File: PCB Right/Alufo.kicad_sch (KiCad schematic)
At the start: 32 parts, among them J2 USB_C_Receptacle_USB2.0_16P_2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, J4 USB_C_Receptacle_USB2.0_16P_2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, J6 SolderHole, SW2 BOOT, U2 CH552T, U4 USBLC6-2P6, U6 USBLC6-2P6

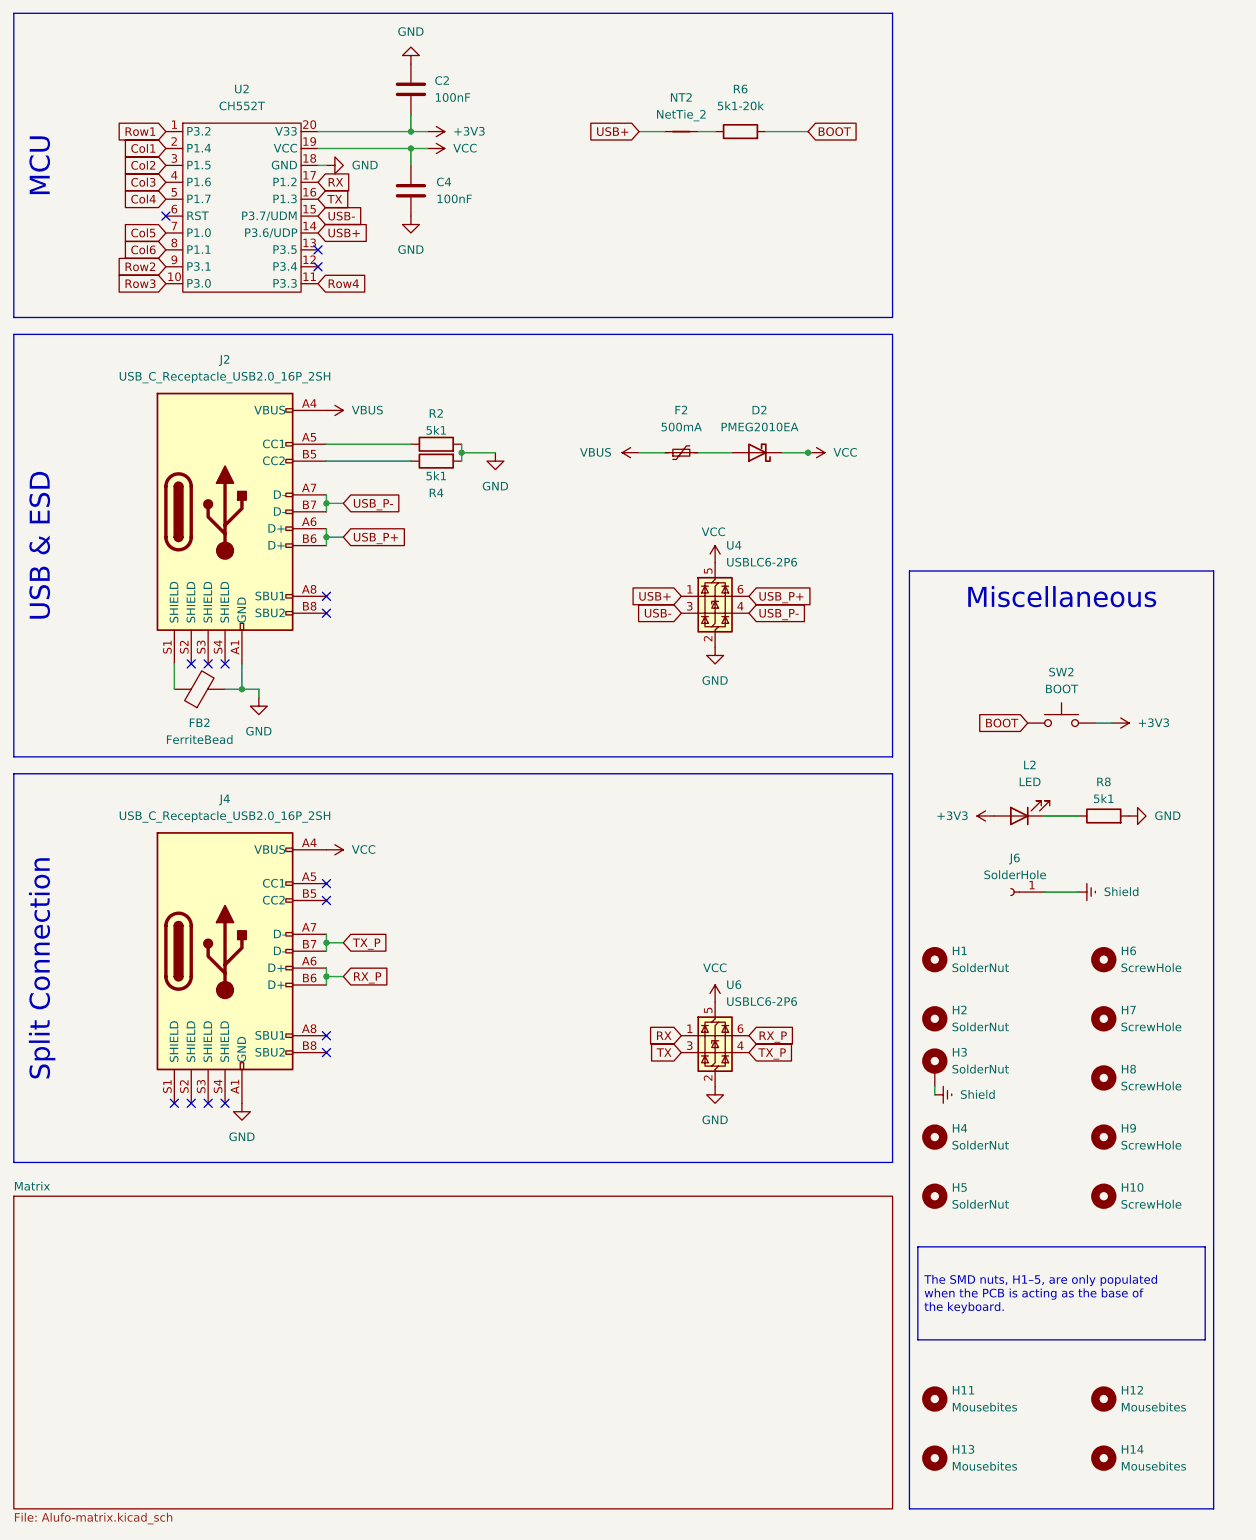
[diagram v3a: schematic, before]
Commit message: Update right side
Also add outline for middle layer to new USB port footprint (although it won’t be right.
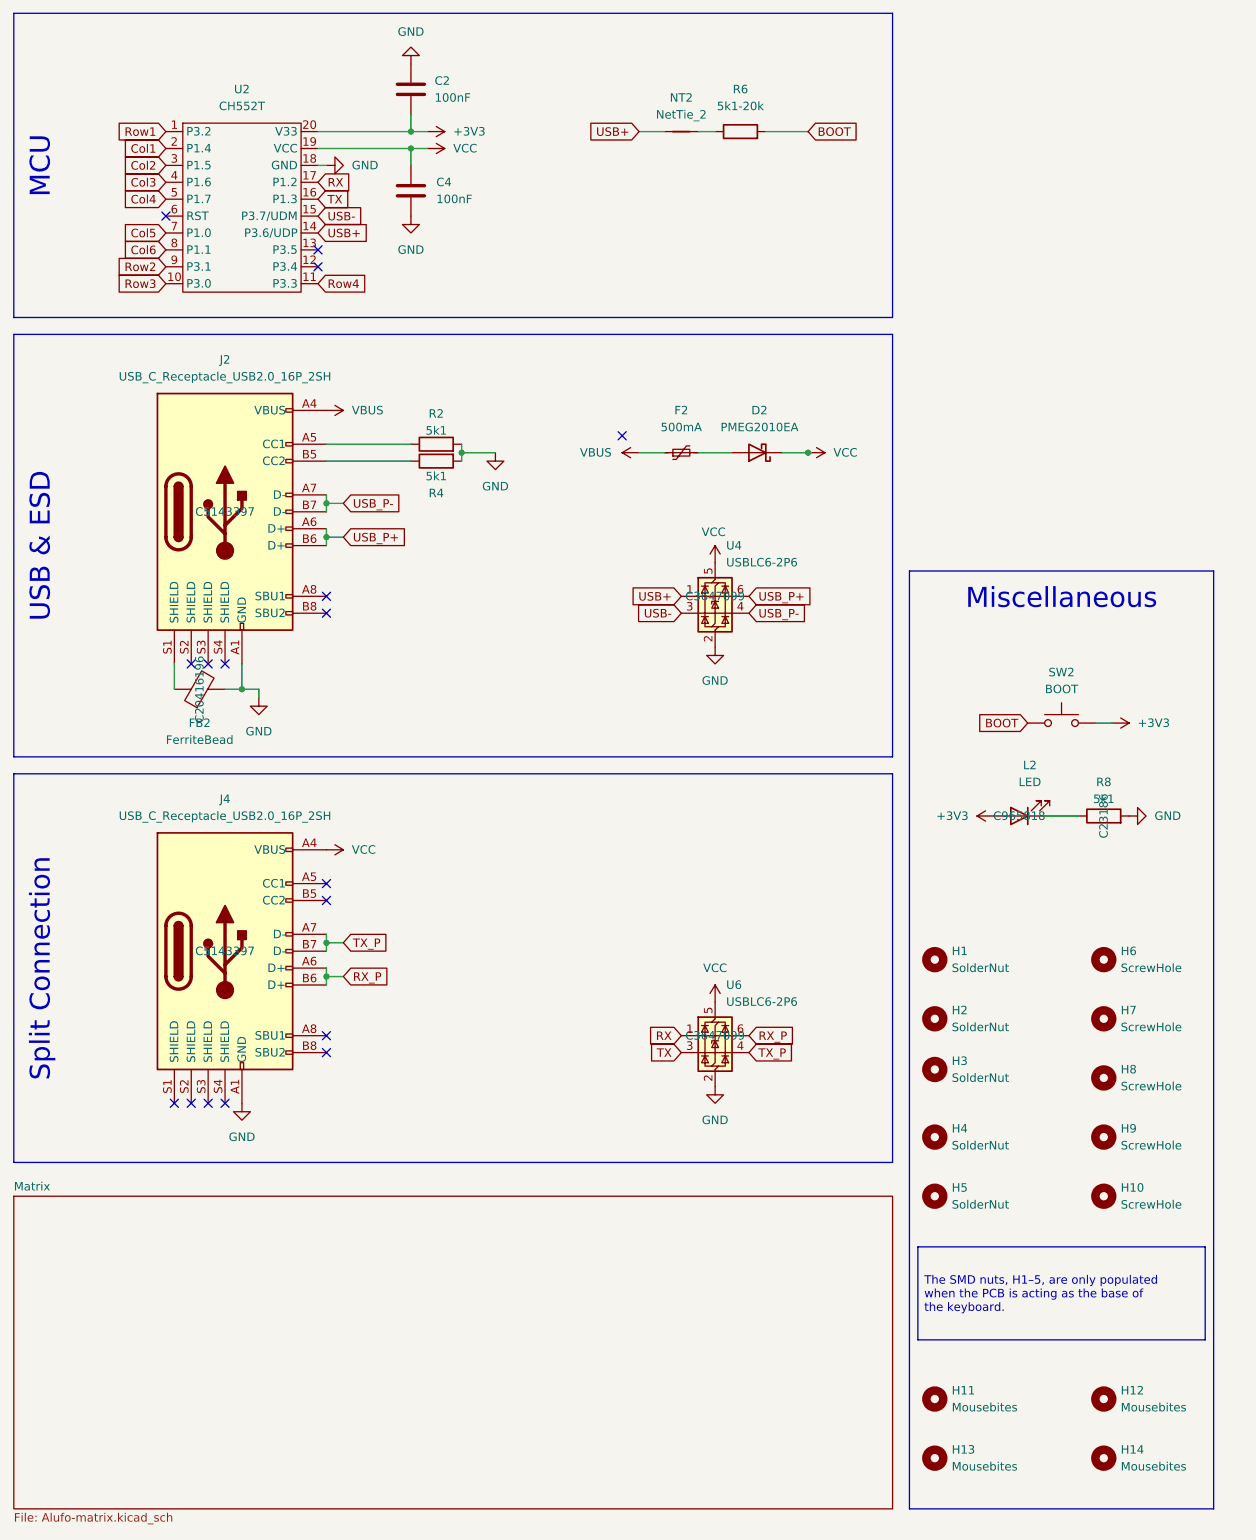
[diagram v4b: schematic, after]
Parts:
- removed J6: SolderHole, Project_Library:TestPoint_THTPad_D2.5mm_Drill1.2mm, symbol Connector:Conn_01x01_Socket
- D2: LCSC C2837790 -> C193668
- FB2: LCSC (none) -> C20416196
- H3: footprint Project_Library:MountingHole_2.2mm_M2_SMD_Solder_Nut_Pad -> Project_Library:MountingHole_2.2mm_M2_SMD_Solder_Nut; symbol Mechanical:MountingHole_Pad -> Mechanical:MountingHole; now left out of the parts list
- J2, J4: footprint Project_Library:USB_C_Receptacle_HRO_TYPE-C-31-M-12 -> Project_Library:USB_C_Receptacle_GCT_USB4110; LCSC (none) -> C5143397
- L2: LCSC (none) -> C965818
- R8: LCSC (none) -> C23186
- U4, U6: LCSC (none) -> C3647099
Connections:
- removed net Shield: H3.1
- no-connect marks 16 -> 17
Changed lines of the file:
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@@
 	(title_block
 		(title "Alufo ")
-		(rev "1.0R")
+		(rev "1.1R")
 		(company "bgkendall")
 		(comment 1 "Split one-layer reversible keyboard PCB (righthand side)")
@@
 	)
 	(no_connect
+		(at 106.68 88.9)
+	)
+	(no_connect
 		(at 62.23 156.21)
 	)
@@
 	(wire
 		(pts
-			(xy 153.67 186.69) (xy 153.67 187.96)
-		)
-		(stroke
-			(width 0)
-			(type default)
-		)
-	)
-	(wire
-		(pts
 			(xy 74.93 40.64) (xy 74.93 43.18)
 		)
@@
 	(wire
 		(pts
-			(xy 170.18 157.48) (xy 175.26 157.48)
-		)
-		(stroke
-			(width 0)
-			(type default)
-		)
-	)
-	(wire
-		(pts
 			(xy 74.93 90.17) (xy 62.23 90.17)
 		)
@@
 			)
 		)
-		(property "Footprint" "Project_Library:USB_C_Receptacle_HRO_TYPE-C-31-M-12"
+		(property "Footprint" "Project_Library:USB_C_Receptacle_GCT_USB4110"
 			(at 50.8 100.33 0)
 			(effects
@@
 			)
 		)
+		(property "LCSC" "C5143397"
+			(at 46.99 100.33 0)
+			(effects
+				(font
+					(size 1.27 1.27)
+				)
+			)
+		)
 		(pin "B8"
 		)
@@
 			)
 		)
-		(property "Footprint" "Project_Library:USB_C_Receptacle_HRO_TYPE-C-31-M-12"
+		(property "Footprint" "Project_Library:USB_C_Receptacle_GCT_USB4110"
 			(at 50.8 166.37 0)
 			(effects
@@
 			)
 		)
+		(property "LCSC" "C5143397"
+			(at 46.99 166.37 0)
+			(effects
+				(font
+					(size 1.27 1.27)
+				)
+			)
+		)
 		(pin "B8"
 		)
@@
 			)
 		)
+		(property "LCSC" "C3647099"
+			(at 120.65 179.07 0)
+			(effects
+				(font
+					(size 1.27 1.27)
+				)
+			)
+		)
 		(pin "4"
 		)
@@
 			)
 		)
+		(property "LCSC" "C965818"
+			(at 166.37 146.05 0)
+			(effects
+				(font
+					(size 1.27 1.27)
+				)
+			)
+		)
 		(pin "1"
 		)
@@
 	)
 	(symbol
-		(lib_id "Connector:Conn_01x01_Socket")
-		(at 165.1 157.48 180)
-		(unit 1)
-		(exclude_from_sim no)
-		(in_bom yes)
-		(on_board yes)
-		(dnp no)
-		(fields_autoplaced yes)
-		(property "Reference" "J6"
-			(at 165.735 152.4 0)
-			(effects
-				(font
-					(size 1.27 1.27)
-				)
-			)
-		)
-		(property "Value" "SolderHole"
-			(at 165.735 154.94 0)
-			(effects
-				(font
-					(size 1.27 1.27)
-				)
-			)
-		)
-		(property "Footprint" "Project_Library:TestPoint_THTPad_D2.5mm_Drill1.2mm"
-			(at 165.1 157.48 0)
-			(effects
-				(font
-					(size 1.27 1.27)
-				)
-				(hide yes)
-			)
-		)
-		(property "Datasheet" "~"
-			(at 165.1 157.48 0)
-			(effects
-				(font
-					(size 1.27 1.27)
-				)
-				(hide yes)
-			)
-		)
-		(property "Description" "Generic connector, single row, 01x01, script generated"
-			(at 165.1 157.48 0)
-			(effects
-				(font
-					(size 1.27 1.27)
-				)
-				(hide yes)
-			)
-		)
-		(pin "1"
-		)
-		(instances
-			(project "Alufo"
-				(path "/52f043ac-ccff-4c85-bc10-2db9d3c9e3f3"
-					(reference "J6")
-					(unit 1)
-				)
-			)
-		)
-	)
-	(symbol
 		(lib_id "power:GND")
 		(at 74.93 33.02 180)
@@
 			)
 		)
+		(property "LCSC" "C20416196"
+			(at 43.18 127 0)
+			(effects
+				(font
+					(size 1.27 1.27)
+				)
+			)
+		)
 		(pin "1"
 		)
@@
 	)
 	(symbol
-		(lib_id "power:Earth")
-		(at 175.26 157.48 90)
-		(unit 1)
-		(exclude_from_sim no)
-		(in_bom yes)
-		(on_board yes)
-		(dnp no)
-		(fields_autoplaced yes)
-		(property "Reference" "#PWR01"
-			(at 181.61 157.48 0)
-			(effects
-				(font
-					(size 1.27 1.27)
-				)
-				(hide yes)
-			)
-		)
-		(property "Value" "Shield"
-			(at 179.07 157.4799 90)
-			(effects
-				(font
-					(size 1.27 1.27)
-				)
-				(justify right)
-			)
-		)
-		(property "Footprint" ""
-			(at 175.26 157.48 0)
-			(effects
-				(font
-					(size 1.27 1.27)
-				)
-				(hide yes)
-			)
-		)
-		(property "Datasheet" "~"
-			(at 175.26 157.48 0)
-			(effects
-				(font
-					(size 1.27 1.27)
-				)
-				(hide yes)
-			)
-		)
-		(property "Description" "Power symbol creates a global label with name \"Earth\""
-			(at 175.26 157.48 0)
-			(effects
-				(font
-					(size 1.27 1.27)
-				)
-				(hide yes)
-			)
-		)
-		(pin "1"
-		)
-		(instances
-			(project "Alufo"
-				(path "/52f043ac-ccff-4c85-bc10-2db9d3c9e3f3"
-					(reference "#PWR01")
-					(unit 1)
-				)
-			)
-		)
-	)
-	(symbol
 		(lib_id "Device:R")
 		(at 78.74 90.17 90)
@@
 			)
 		)
+		(property "LCSC" "C3647099"
+			(at 120.65 113.03 0)
+			(effects
+				(font
+					(size 1.27 1.27)
+				)
+			)
+		)
 		(pin "4"
 		)
@@
 	)
 	(symbol
-		(lib_id "Mechanical:MountingHole_Pad")
+		(lib_name "MountingHole_1")
+		(lib_id "Mechanical:MountingHole")
 		(at 153.67 184.15 0)
 		(unit 1)
 		(exclude_from_sim yes)
-		(in_bom yes)
+		(in_bom no)
 		(on_board yes)
 		(dnp no)
 		(fields_autoplaced yes)
 		(property "Reference" "H3"
-			(at 156.21 181.6099 0)
+			(at 156.21 182.88 0)
 			(effects
 				(font
@@
 		)
 		(property "Value" "SolderNut"
-			(at 156.21 184.1499 0)
+			(at 156.21 185.42 0)
 			(effects
 				(font
@@
 			)
 		)
-		(property "Footprint" "Project_Library:MountingHole_2.2mm_M2_SMD_Solder_Nut_Pad"
+		(property "Footprint" "Project_Library:MountingHole_2.2mm_M2_SMD_Solder_Nut"
 			(at 153.67 184.15 0)
 			(effects
@@
 			)
 		)
-		(property "Description" "Mounting Hole with connection"
+		(property "Description" "Mounting Hole without connection"
 			(at 153.67 184.15 0)
 			(effects
@@
 			)
 		)
-		(pin "1"
-		)
 		(instances
 			(project "Alufo"
@@
 	)
 	(symbol
-		(lib_id "power:Earth")
-		(at 153.67 187.96 90)
-		(unit 1)
-		(exclude_from_sim no)
-		(in_bom yes)
-		(on_board yes)
-		(dnp no)
-		(fields_autoplaced yes)
-		(property "Reference" "#PWR02"
-			(at 160.02 187.96 0)
-			(effects
-				(font
-					(size 1.27 1.27)
-				)
-				(hide yes)
-			)
-		)
-		(property "Value" "Shield"
-			(at 157.48 187.9599 90)
-			(effects
-				(font
-					(size 1.27 1.27)
-				)
-				(justify right)
-			)
-		)
-		(property "Footprint" ""
-			(at 153.67 187.96 0)
-			(effects
-				(font
-					(size 1.27 1.27)
-				)
-				(hide yes)
-			)
-		)
-		(property "Datasheet" "~"
-			(at 153.67 187.96 0)
-			(effects
-				(font
-					(size 1.27 1.27)
-				)
-				(hide yes)
-			)
-		)
-		(property "Description" "Power symbol creates a global label with name \"Earth\""
-			(at 153.67 187.96 0)
-			(effects
-				(font
-					(size 1.27 1.27)
-				)
-				(hide yes)
-			)
-		)
-		(pin "1"
-		)
-		(instances
-			(project "Alufo"
-				(path "/52f043ac-ccff-4c85-bc10-2db9d3c9e3f3"
-					(reference "#PWR02")
-					(unit 1)
-				)
-			)
-		)
-	)
-	(symbol
 		(lib_id "Mechanical:MountingHole")
 		(at 179.07 194.31 0)
@@
 			)
 		)
+		(property "LCSC" "C23186"
+			(at 179.07 146.05 0)
+			(effects
+				(font
+					(size 1.27 1.27)
+				)
+			)
+		)
 		(pin "2"
 		)
@@
 			)
 		)
-		(property "LCSC" "C2837790"
+		(property "LCSC" "C193668"
 			(at 127 91.44 0)
 			(effects

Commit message: Add ferrite bead to righthand side split connector port
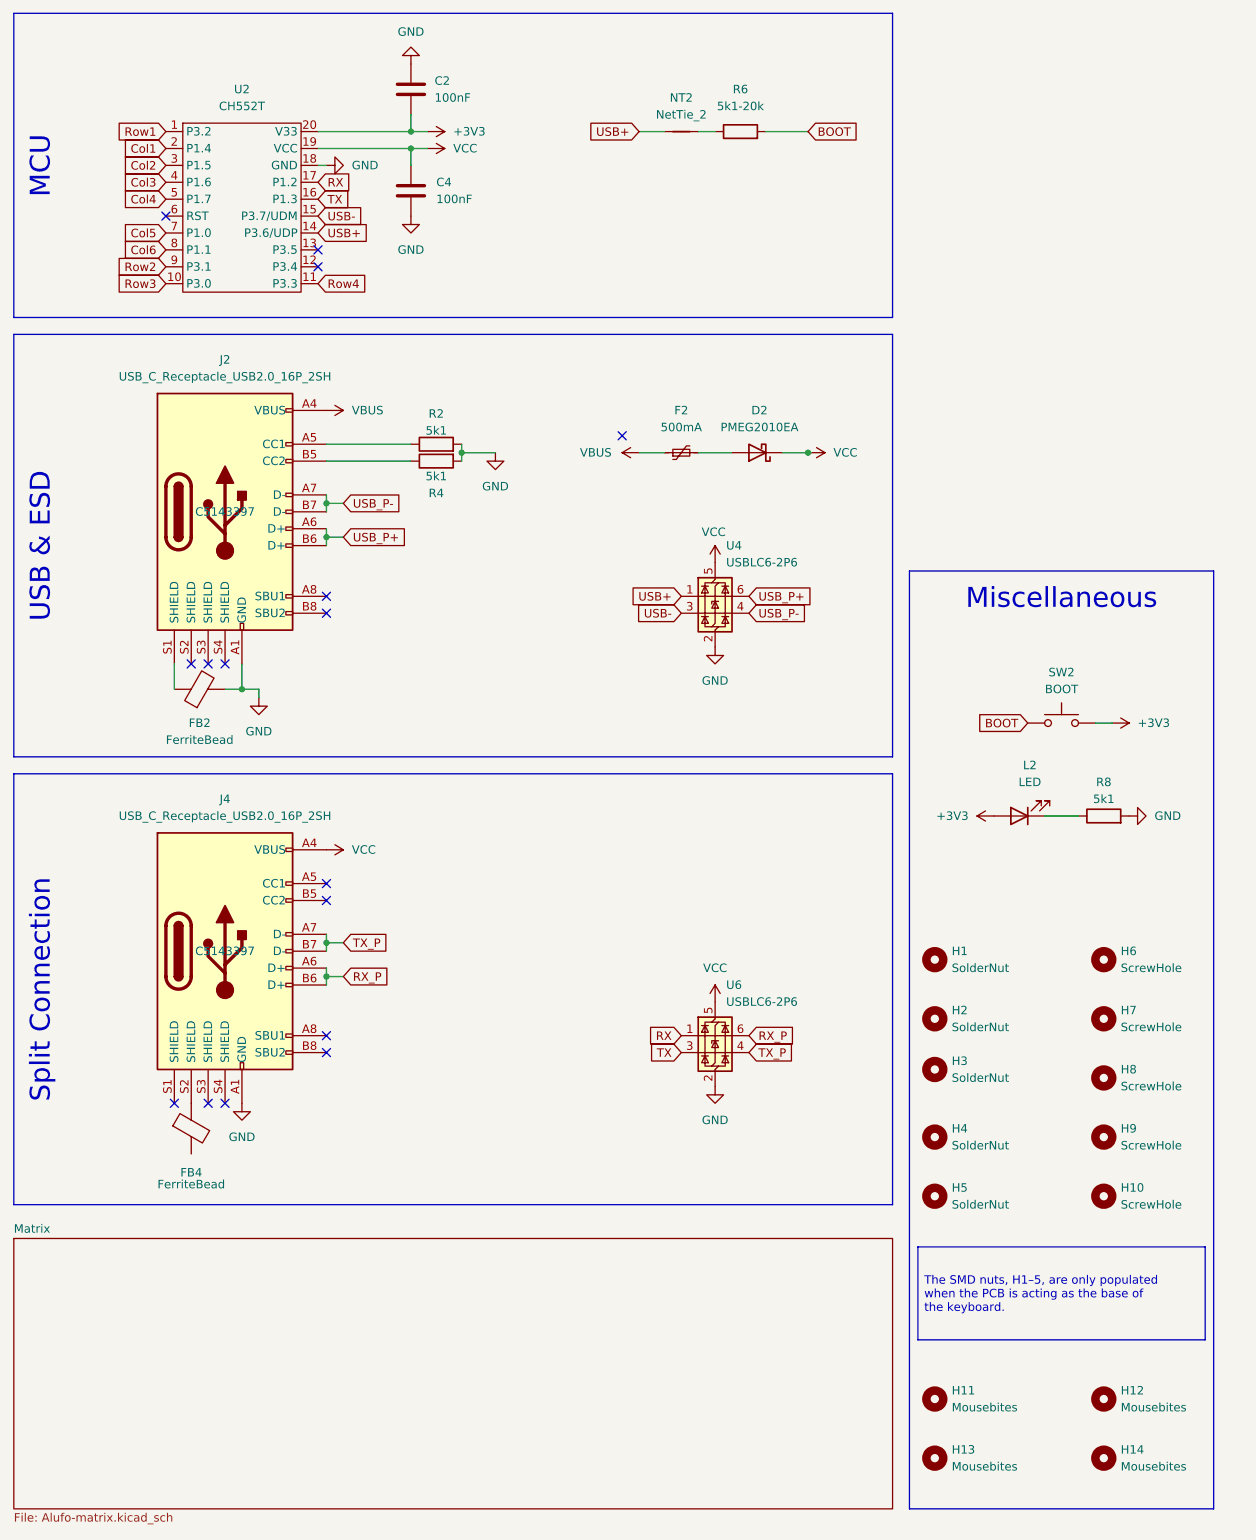
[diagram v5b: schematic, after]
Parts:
- added FB4: FerriteBead, Inductor_SMD:L_0805_2012Metric, symbol Device:FerriteBead
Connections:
- net at J4.S2 (SHIELD): now also FB4.1
- no-connect marks 17 -> 16
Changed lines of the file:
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@@
 		(exclude_from_sim no)
 		(at 15.24 139.7 90)
-		(size 132.08 58.42)
+		(size 132.08 64.77)
 		(margins 2.25 2.25 2.25 2.25)
 		(stroke
@@
 	)
 	(no_connect
-		(at 41.91 189.23)
-	)
-	(no_connect
 		(at 62.23 181.61)
 	)
@@
 					(size 1.27 1.27)
 				)
+				(hide yes)
 			)
 		)
@@
 					(size 1.27 1.27)
 				)
+				(hide yes)
 			)
 		)
@@
 					(size 1.27 1.27)
 				)
+				(hide yes)
 			)
 		)
@@
 					(size 1.27 1.27)
 				)
+				(hide yes)
 			)
 		)
@@
 					(size 1.27 1.27)
 				)
+				(hide yes)
 			)
 		)
@@
 		)
 	)
+	(symbol
+		(lib_id "Device:FerriteBead")
+		(at 41.91 193.04 0)
+		(unit 1)
+		(exclude_from_sim no)
+		(in_bom yes)
+		(on_board yes)
+		(dnp no)
+		(property "Reference" "FB4"
+			(at 41.91 199.644 0)
+			(effects
+				(font
+					(size 1.27 1.27)
+				)
+			)
+		)
+		(property "Value" "FerriteBead"
+			(at 41.91 201.422 0)
+			(effects
+				(font
+					(size 1.27 1.27)
+				)
+			)
+		)
+		(property "Footprint" "Inductor_SMD:L_0805_2012Metric"
+			(at 40.132 193.04 90)
+			(effects
+				(font
+					(size 1.27 1.27)
+				)
+				(hide yes)
+			)
+		)
+		(property "Datasheet" "~"
+			(at 41.91 193.04 0)
+			(effects
+				(font
+					(size 1.27 1.27)
+				)
+				(hide yes)
+			)
+		)
+		(property "Description" "Ferrite bead"
+			(at 41.91 193.04 0)
+			(effects
+				(font
+					(size 1.27 1.27)
+				)
+				(hide yes)
+			)
+		)
+		(property "LCSC" "C20416196"
+			(at 41.91 193.04 0)
+			(effects
+				(font
+					(size 1.27 1.27)
+				)
+				(hide yes)
+			)
+		)
+		(pin "1"
+		)
+		(pin "2"
+		)
+		(instances
+			(project "Alufo"
+				(path "/52f043ac-ccff-4c85-bc10-2db9d3c9e3f3"
+					(reference "FB4")
+					(unit 1)
+				)
+			)
+		)
+	)
 	(sheet
-		(at 15.24 203.2)
-		(size 132.08 46.99)
+		(at 15.24 209.55)
+		(size 132.08 40.64)
 		(exclude_from_sim no)
 		(in_bom yes)
@@
 		)
 		(property "Sheetname" "Matrix"
-			(at 15.24 202.4884 0)
+			(at 15.24 208.8384 0)
 			(effects
 				(font
